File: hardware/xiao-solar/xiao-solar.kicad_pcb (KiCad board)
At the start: 2 copper layers, 48 x 94 mm, 85 parts, among them J1 SOLAR, J2 VIN2 5-20V, J3 NTC 10k (103AT), J4 BATTERY, J5 I2C rail, J7 OUT1 heater, J8 OUT2 fan, J9 OUT3 spare, Q2 AO3400A (ship FET), Q3 HJ8205, Q4 AO3400A, Q5 AO3400A, Q6 AO3400A, U1 BQ25798RQMR, U2 DW01A, U3 XIAO nRF52840, U4 Wio-SX1262 for XIAO, U5 SHT40-AD1B, U6 PCA9685PW

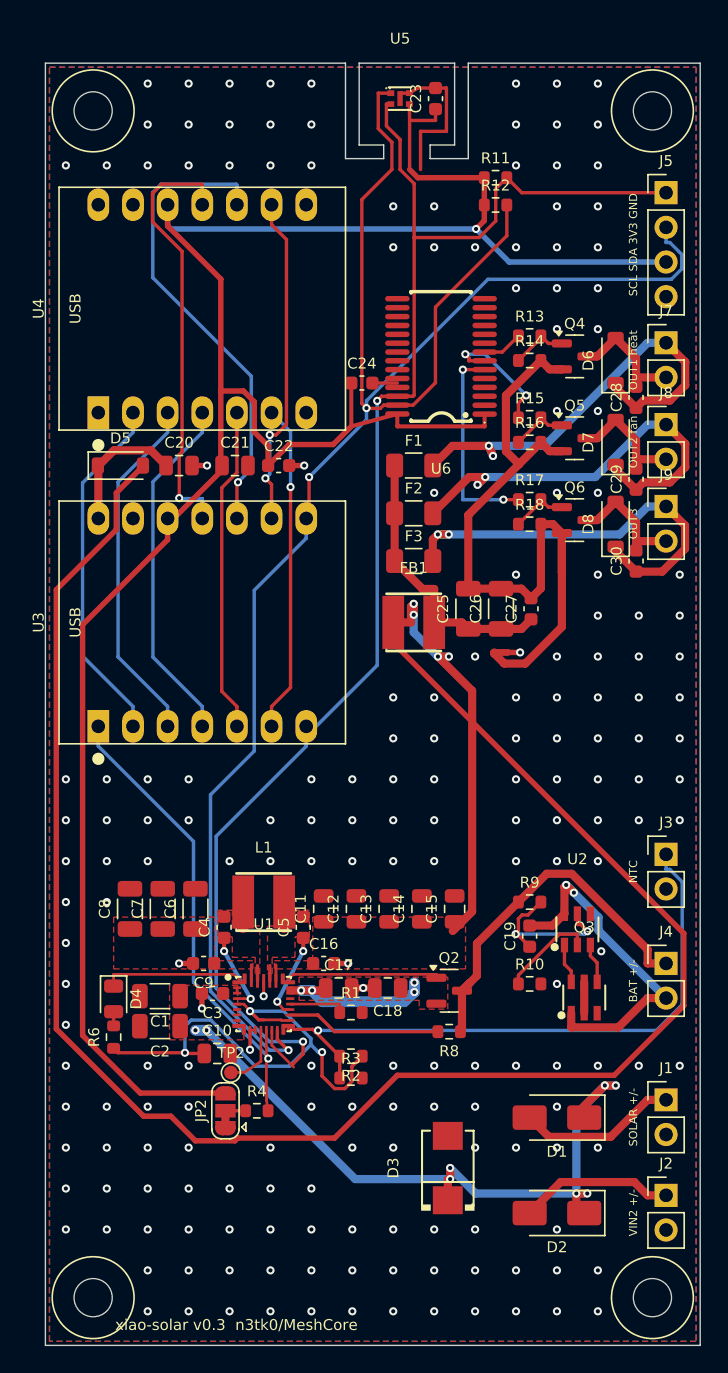
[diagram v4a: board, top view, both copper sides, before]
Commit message: hardware: xiao-solar v0.4 (no loads, INA219, 48x71.5) + block schematics for both boards
Co-Authored-By: Claude Opus 5.5 <noreply@anthropic.com>
Claude-Session: https://claude.ai/code/session_01P5Km81NY9NPL6RpKFGVEbH
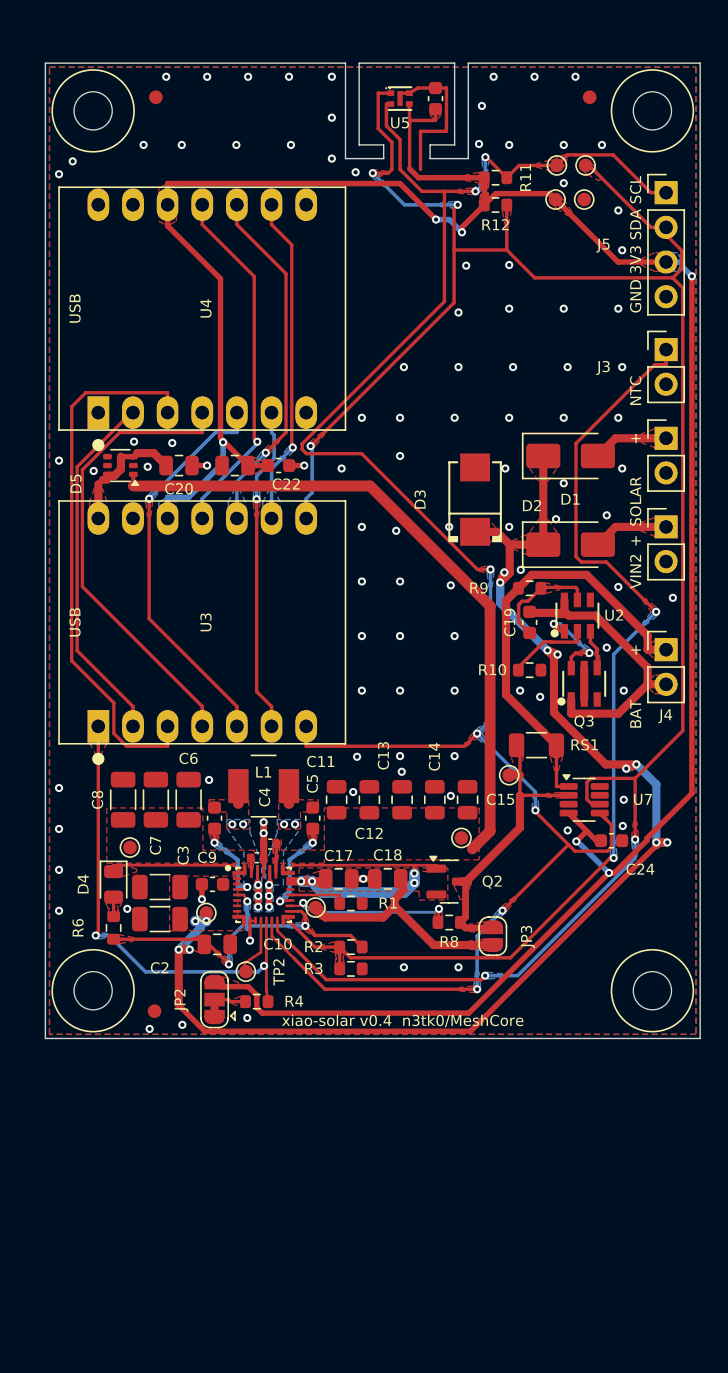
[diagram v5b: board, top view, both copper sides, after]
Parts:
- removed C25, C26: 22u/25V, Capacitor_SMD:C_1206_3216Metric
- removed C27, C28, C29, C30: 100n, Capacitor_SMD:C_0603_1608Metric
- removed D6, D7, D8: B5819W, Diode_SMD:D_SOD-123
- removed F1, F2, F3: 2A/16V, Fuse:Fuse_1206_3216Metric
- removed FB1: 2.2uH 3.2A, xiao_solar:IND-SMD_L4.0-W4.0_FNR40XXS
- removed J7: OUT1 heater, Connector_PinHeader_2.54mm:PinHeader_1x02_P2.54mm_Vertical
- removed J8: OUT2 fan, Connector_PinHeader_2.54mm:PinHeader_1x02_P2.54mm_Vertical
- removed J9: OUT3 spare, Connector_PinHeader_2.54mm:PinHeader_1x02_P2.54mm_Vertical
- removed NT1: PGND-GND, NetTie:NetTie-2_SMD_Pad0.5mm
- removed Q4, Q5, Q6: AO3400A, Package_TO_SOT_SMD:SOT-23
- removed R13, R15, R17: 1k, Resistor_SMD:R_0603_1608Metric
- removed R14, R16, R18: 100k, Resistor_SMD:R_0603_1608Metric
- removed U6: PCA9685PW, xiao_solar:TSSOP-28_L9.7-W4.4-P0.65-LS6.4-TL
- added FID1: Fiducial, Fiducial_1mm_Mask2mm, F.Cu at (108.1, 102.5)
- added FID2: Fiducial, Fiducial_1mm_Mask2mm, F.Cu at (139.9, 102.5)
- added FID3: Fiducial, Fiducial_1mm_Mask2mm, F.Cu at (108.0, 169.5)
- added JP3: no ship FET (LiFePO4), Jumper:SolderJumper-2_P1.3mm_Open_RoundedPad1.0x1.5mm, F.Cu at (132.8, 164.0)
- added RS1: 0.05 1W, Resistor_SMD:R_1206_3216Metric, F.Cu at (136.0, 150.0)
- added TP10: SDA, TestPoint:TestPoint_Pad_D1.0mm, F.Cu at (139.6, 107.5)
- added TP11: BATS, TestPoint:TestPoint_Pad_D1.0mm, F.Cu at (134.0, 152.2)
- added TP3: VBUS, TestPoint:TestPoint_Pad_D1.0mm, F.Cu at (111.8, 162.3)
- added TP4: PMID, TestPoint:TestPoint_Pad_D1.0mm, F.Cu at (106.2, 157.5)
- added TP5: SYS, TestPoint:TestPoint_Pad_D1.0mm, F.Cu at (130.5, 156.8)
- added TP6: BAT, TestPoint:TestPoint_Pad_D1.0mm, F.Cu at (119.8, 161.9)
- added TP7: GND, TestPoint:TestPoint_Pad_D1.0mm, F.Cu at (139.5, 110.0)
- added TP8: 3V3, TestPoint:TestPoint_Pad_D1.0mm, F.Cu at (137.4, 110.0)
- added TP9: SCL, TestPoint:TestPoint_Pad_D1.0mm, F.Cu at (137.5, 107.5)
- added U7: INA219AIDCNR, Package_TO_SOT_SMD:SOT-23-8, F.Cu at (139.5, 154.0)
- C16: footprint Capacitor_SMD:C_0603_1608Metric -> Capacitor_SMD:C_0402_1005Metric
- C9: value 100n -> 100n/50V; footprint Capacitor_SMD:C_0603_1608Metric -> Capacitor_SMD:C_0402_1005Metric
- D1, D2: value SS34 -> SS54
- D5: value B5819W -> LM66100; footprint Diode_SMD:D_SOD-123 -> Package_TO_SOT_SMD:SOT-363_SC-70-6
- L1: value 2.2uH 3.2A -> 2.2uH 4A molded (MWSA0402S); footprint xiao_solar:IND-SMD_L4.0-W4.0_FNR40XXS -> xiao_solar:IND-SMD_L4.4-W4.2_MWSA0402S
- moved D3 49.0 mm to (131.5, 132.0)
- moved D2 49.0 mm to (138.5, 135.3), turned to 0 degrees
- moved J2 49.0 mm to (145.5, 134.0)
- moved D1 48.5 mm to (138.5, 128.8), turned to 0 degrees
- moved J1 48.5 mm to (145.5, 127.5)
- moved C24 38.2 mm to (141.5, 157.0)
- moved J3 37.0 mm to (145.5, 121.0)
- moved C19 23.0 mm to (135.5, 141.0)
- moved J4 23.0 mm to (145.5, 143.0)
- moved Q3 23.0 mm to (139.5, 145.5)
- moved R10 23.0 mm to (135.5, 144.5)
- moved R9 23.0 mm to (135.5, 138.5)
- moved U2 23.0 mm to (139.0, 140.5)
- moved H3 22.5 mm to (103.5, 168.0)
- moved H4 22.5 mm to (144.5, 168.0)
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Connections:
- D5 pad 1: XIAO_5V -> SYS
- D5 pad 2: SYS -> GND
- Q2 pad 3: BATT+ -> BATS
- R8 pad 1: BATT+ -> BATS
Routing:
- net SYS: track 167.0 -> 51.0 mm, vias 4 -> 0
- net PGND: track 54.3 -> 0.00 mm
- net VBUS: track 52.8 -> 98.6 mm, vias 8 -> 12
- net SCL: track 109.6 -> 146.7 mm, vias 2 -> 7
- net OUT1+: track 32.9 -> 0.00 mm, vias 2 -> 0
- net OUT2+: track 31.8 -> 0.00 mm, vias 2 -> 0
- net OUT3+: track 31.7 -> 0.00 mm, vias 2 -> 0
- net TS: track 45.6 -> 74.9 mm, vias 1 -> 2
- net SDA: track 134.7 -> 158.4 mm, vias 3 -> 5
- net BATS: track 0.00 -> 22.1 mm
- net VLOAD: track 20.8 -> 0.00 mm
- net BAT: track 12.6 -> 28.9 mm
- net 3V3: track 165.9 -> 181.5 mm, vias 1 -> 6
- net PWM3: track 15.2 -> 0.00 mm, vias 2 -> 0
- net LORA_RST: track 26.0 -> 39.9 mm
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- added copper zone on B.Cu, net 3V3
- added copper zone on F.Cu, net 3V3
- added copper zone on B.Cu, net BATP
- added copper zone on F.Cu, net BATP
- added copper zone on F.Cu, net BATS
- added copper zone on F.Cu, net BATT+
- added copper zone on F.Cu, net BATT-
- added copper zone on B.Cu, net BTST1
- added copper zone on F.Cu, net BTST1
- added copper zone on B.Cu, net BTST2
- added copper zone on F.Cu, net BTST2
- added copper zone on B.Cu, net CE
- added copper zone on F.Cu, net CE
- added copper zone on F.Cu, net CE_PULL
- added copper zone on F.Cu, net DW_OC
- added copper zone on B.Cu, net DW_OD
- added copper zone on F.Cu, net DW_OD
- added copper zone on F.Cu, net DW_VCC
- added copper zone on F.Cu, net LED_STAT
- added copper zone on B.Cu, net LORA_NSS
- added copper zone on F.Cu, net LORA_NSS
- added copper zone on B.Cu, net LORA_RXEN
- added copper zone on F.Cu, net LORA_RXEN
- added copper zone on B.Cu, net REGN
- added copper zone on F.Cu, net REGN
- added copper zone on B.Cu, net SCL
- added copper zone on F.Cu, net SCL
- added copper zone on B.Cu, net SDA
- added copper zone on F.Cu, net SDA
- added copper zone on F.Cu, net SDRV
- added copper zone on F.Cu, net SOLAR_IN
- added copper zone on B.Cu, net SPI_MISO
- added copper zone on F.Cu, net SPI_MISO
- added copper zone on B.Cu, net SPI_SCK
- added copper zone on F.Cu, net STAT
- added copper zone on B.Cu, net SW1
- added copper zone on B.Cu, net SW2
- added copper zone on B.Cu, net TS
- added copper zone on F.Cu, net TS
- added copper zone on F.Cu, net VIN2_IN
- added copper zone on F.Cu, net XIAO_5V
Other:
- board size 48 x 94 mm -> 48 x 71.5 mm
- board text added: "+"
- board text added: "BAT"
- board text added: "GND 3V3 SDA SCL"
- board text added: "SOLAR"
- board text added: "VIN2"
- board text added: "xiao-solar v0.4 n3tk0/MeshCore"
- board text removed: "BAT +/-"
- board text removed: "OUT1 heat"
- board text removed: "OUT2 fan"
- board text removed: "OUT3"
- board text removed: "SCL SDA 3V3 GND"
- board text removed: "SOLAR +/-"
- board text removed: "VIN2 +/-"
- board text removed: "xiao-solar v0.3 n3tk0/MeshCore"
